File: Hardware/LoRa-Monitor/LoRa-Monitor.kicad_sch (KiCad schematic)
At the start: 0 parts

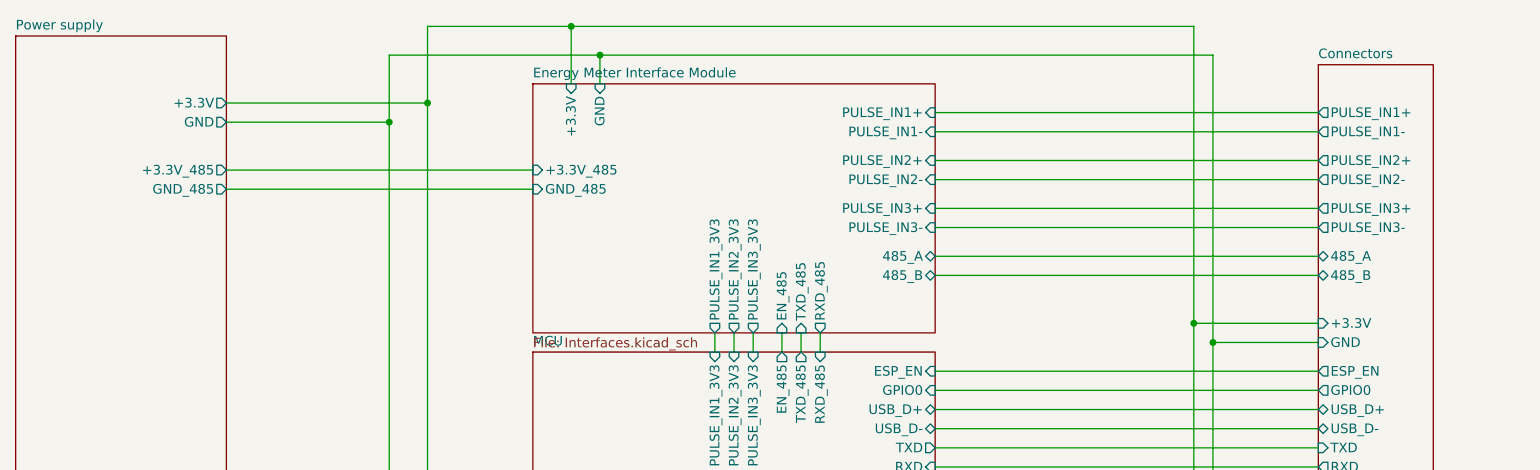
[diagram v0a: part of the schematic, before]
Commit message: Changed the RS485-TTL translator and its relevent componentes (Power source and optocuplers) for a simpler and easier solution using the ADM2582.
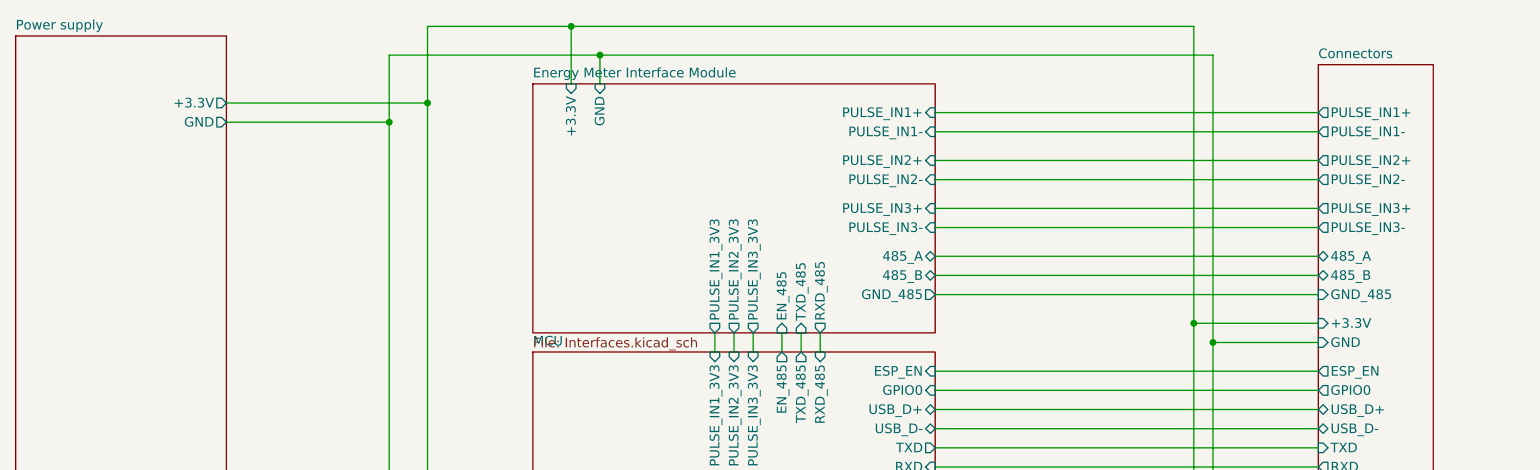
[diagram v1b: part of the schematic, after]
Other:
- sheet Connectors ports: added GND_485; removed none
- sheet Energy Meter Interface Module ports: added none; removed +3.3V_485
- sheet Power supply ports: added none; removed +3.3V_485, GND_485
